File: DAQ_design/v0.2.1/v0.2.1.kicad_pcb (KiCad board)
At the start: 2 copper layers, 48.7 x 79.5 mm, 19 parts, among them J1 Barrel_Jack, J3 Conn_01x04_Female, J4 Conn_01x05_Female, Q1 BC549, Q2 IRF9540N, Q3 IRF540N, Q4 BC549, Q5 IRF9540N, Q6 IRF540N, U3 ADS1115IDGS

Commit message: updated foorprints
updated footprints
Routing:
- net AIN0: track 110.3 -> 114.4 mm
- net VDD: track 41.5 -> 37.5 mm
- net LOGIC1: track 97.2 -> 96.2 mm
- net SP: track 37.4 -> 36.8 mm

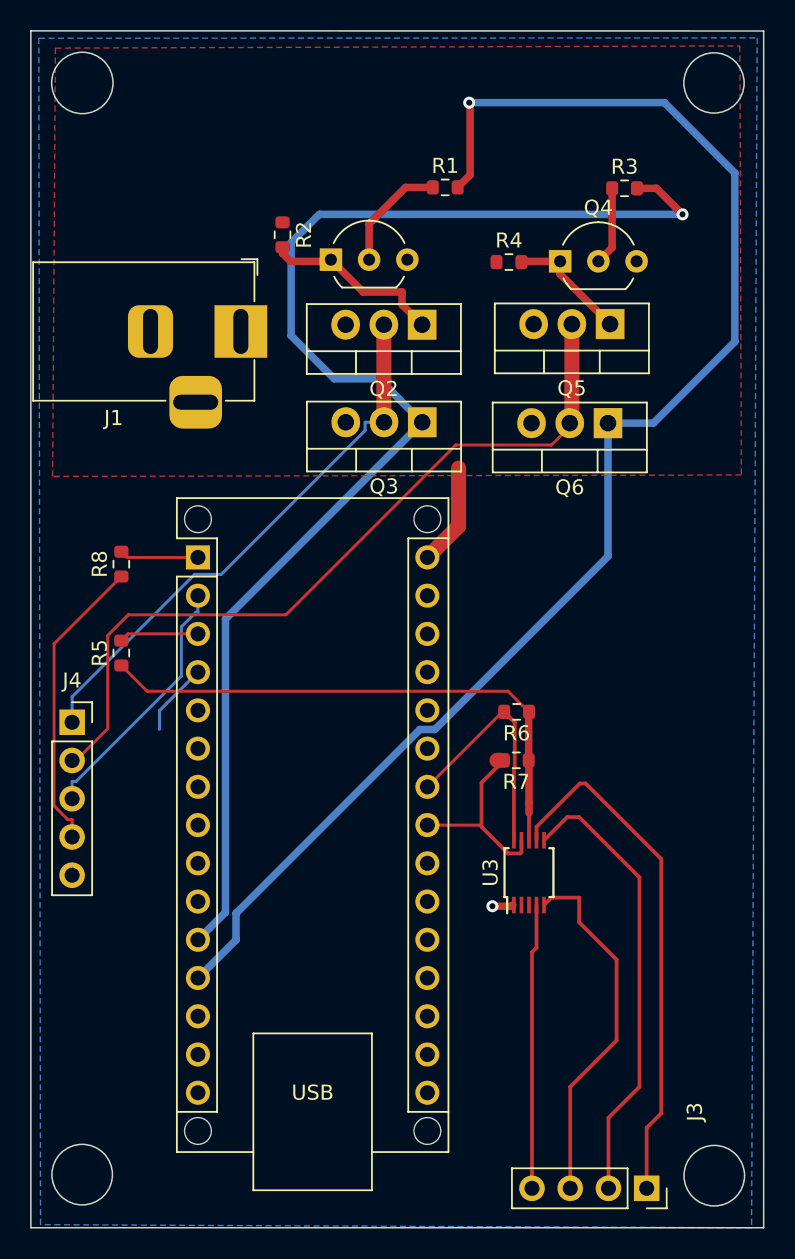
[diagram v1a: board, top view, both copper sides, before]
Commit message: fixed ground plane issue
fixed ground plane issue
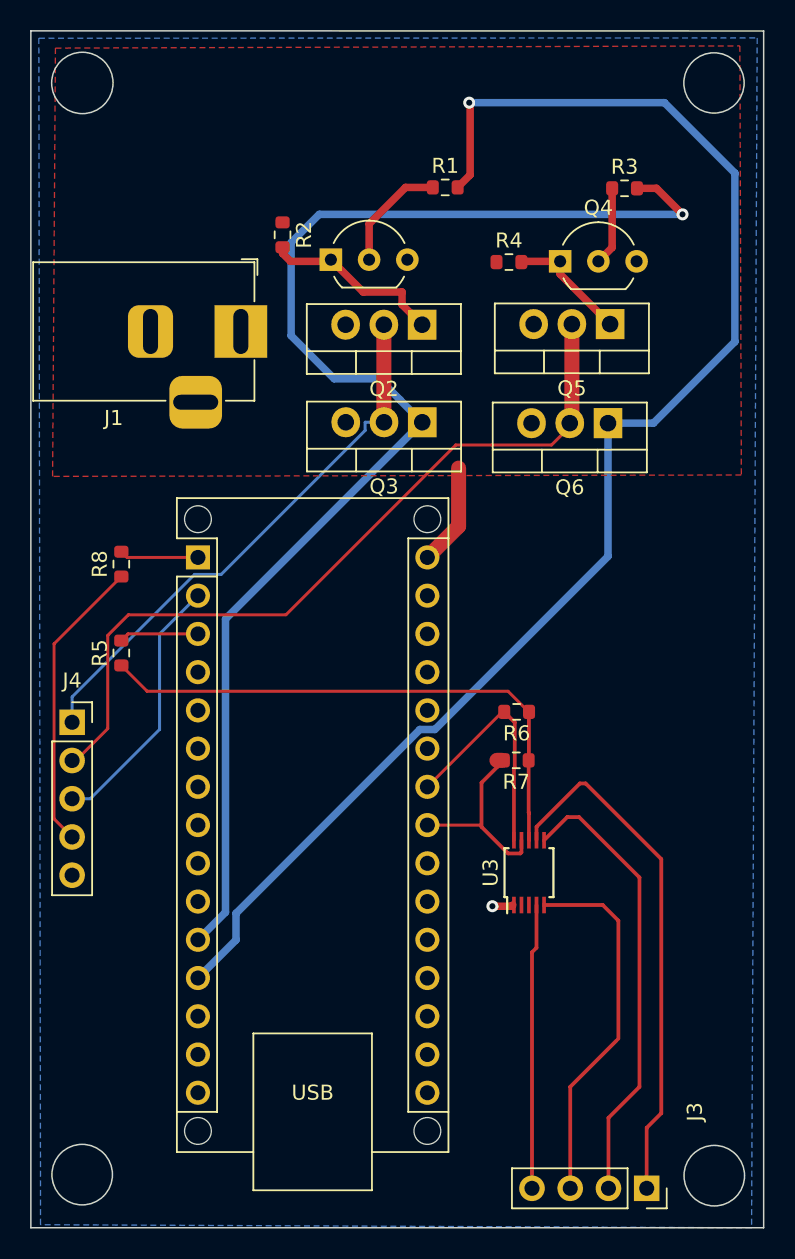
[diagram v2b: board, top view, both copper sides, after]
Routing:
- net AIN0: track 114.4 -> 109.8 mm
- net VDD: track 37.5 -> 37.0 mm
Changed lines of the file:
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@@
   (segment (start 66.485 54.61) (end 71.13 54.61) (width 0.2) (layer "F.Cu") (net 1))
   (segment (start 66.04 55.055) (end 66.485 54.61) (width 0.2) (layer "F.Cu") (net 1))
-  (segment (start 93.1 63.01) (end 93.1 59.815) (width 0.5) (layer "F.Cu") (net 8))
-  (segment (start 93.12 66.51) (end 93.12 65.87) (width 0.25) (layer "F.Cu") (net 8))
+  (segment (start 93.12 66.51) (end 93.1 66.49) (width 0.25) (layer "F.Cu") (net 8))
+  (segment (start 93.1125 62.9975) (end 93.1125 59.8025) (width 0.25) (layer "F.Cu") (net 8))
   (segment (start 91.73 58.42) (end 67.755 58.42) (width 0.2) (layer "F.Cu") (net 8))
+  (segment (start 93.1 63.01) (end 93.1125 62.9975) (width 0.25) (layer "F.Cu") (net 8))
   (segment (start 93.12 68.32) (end 93.12 66.51) (width 0.25) (layer "F.Cu") (net 8))
+  (segment (start 93.1 66.49) (end 93.1 63.01) (width 0.25) (layer "F.Cu") (net 8))
   (segment (start 67.755 58.42) (end 66.04 56.705) (width 0.2) (layer "F.Cu") (net 8))
-  (segment (start 93.12 66.51) (end 93.12 65.87) (width 0.5) (layer "F.Cu") (net 8))
   (segment (start 93.1125 59.8025) (end 91.73 58.42) (width 0.2) (layer "F.Cu") (net 8))
   (segment (start 93.1 59.815) (end 93.1125 59.8025) (width 0.5) (layer "F.Cu") (net 8))
   (segment (start 93.12 63.03) (end 93.1 63.01) (width 0.5) (layer "F.Cu") (net 8))
   (segment (start 93.1125 59.8025) (end 93.125 59.79) (width 0.5) (layer "F.Cu") (net 8))
-  (segment (start 93.12 65.87) (end 93.12 63.03) (width 0.5) (layer "F.Cu") (net 8))
-  (segment (start 96.45 73.76) (end 98.94 76.25) (width 0.25) (layer "F.Cu") (net 9))
   (segment (start 100.46 84.7) (end 100.46 70.79) (width 0.25) (layer "F.Cu") (net 9))
   (segment (start 92.005 72.66) (end 92.045 72.62) (width 0.5) (layer "F.Cu") (net 9))
   (segment (start 98.94 81.62) (end 95.86 84.7) (width 0.25) (layer "F.Cu") (net 9))
   (segment (start 96.885 64.545) (end 96.5 64.545) (width 0.25) (layer "F.Cu") (net 9))
-  (segment (start 94.61 72.13) (end 94.12 72.62) (width 0.25) (layer "F.Cu") (net 9))
   (segment (start 92.08 72.66) (end 92.12 72.62) (width 0.2) (layer "F.Cu") (net 9))
   (segment (start 93.32 75.76) (end 93.62 75.46) (width 0.25) (layer "F.Cu") (net 9))
   (segment (start 100.46 70.79) (end 96.45 66.78) (width 0.25) (layer "F.Cu") (net 9))
   (segment (start 100.94 91.44) (end 100.94 87.42) (width 0.25) (layer "F.Cu") (net 9))
-  (segment (start 96.45 72.13) (end 94.61 72.13) (width 0.25) (layer "F.Cu") (net 9))
-  (segment (start 96.45 72.13) (end 96.45 73.76) (width 0.25) (layer "F.Cu") (net 9))
+  (segment (start 99.06 81.5) (end 98.94 81.62) (width 0.2) (layer "F.Cu") (net 9))
   (segment (start 96.5 64.545) (end 93.62 67.425) (width 0.25) (layer "F.Cu") (net 9))
   (segment (start 93.62 67.425) (end 93.62 68.32) (width 0.25) (layer "F.Cu") (net 9))
@@
   (segment (start 93.62 72.62) (end 93.62 75.46) (width 0.25) (layer "F.Cu") (net 9))
   (segment (start 101.91 69.57) (end 96.885 64.545) (width 0.25) (layer "F.Cu") (net 9))
-  (segment (start 98.94 76.25) (end 98.94 81.62) (width 0.25) (layer "F.Cu") (net 9))
   (segment (start 101.91 86.45) (end 101.91 69.57) (width 0.25) (layer "F.Cu") (net 9))
   (segment (start 91.965 72.7) (end 92.005 72.66) (width 0.5) (layer "F.Cu") (net 9))
+  (segment (start 94.12 72.62) (end 98.02 72.62) (width 0.25) (layer "F.Cu") (net 9))
   (segment (start 100.94 87.42) (end 101.91 86.45) (width 0.25) (layer "F.Cu") (net 9))
   (segment (start 98.4 86.76) (end 100.46 84.7) (width 0.25) (layer "F.Cu") (net 9))
+  (segment (start 98.02 72.62) (end 99.06 73.66) (width 0.25) (layer "F.Cu") (net 9))
   (segment (start 92.005 72.66) (end 92.08 72.66) (width 0.2) (layer "F.Cu") (net 9))
   (segment (start 98.4 91.44) (end 98.4 86.76) (width 0.25) (layer "F.Cu") (net 9))
+  (segment (start 99.06 73.66) (end 99.06 81.5) (width 0.25) (layer "F.Cu") (net 9))
   (via (at 90.69 72.7) (size 0.8) (drill 0.4) (layers "F.Cu" "B.Cu") (net 9))
-  (segment (start 71.13 57.15) (end 68.58 59.7) (width 0.2) (layer "B.Cu") (net 9))
-  (segment (start 68.58 59.7) (end 68.58 60.96) (width 0.2) (layer "B.Cu") (net 9))
   (segment (start 88.4437 47.4563) (end 86.37 49.53) (width 1) (layer "F.Cu") (net 10))
   (segment (start 88.4437 43.596) (end 88.4437 47.4563) (width 1) (layer "F.Cu") (net 10))
@@
   (segment (start 106.8 24) (end 106.8 35.2) (width 0.5) (layer "B.Cu") (net 15))
   (segment (start 106.8 35.2) (end 101.39 40.61) (width 0.5) (layer "B.Cu") (net 15))
-  (segment (start 63.0385 64.4081) (end 62.77 64.4081) (width 0.2) (layer "B.Cu") (net 16))
-  (segment (start 70.0281 54.1359) (end 70.0281 57.4185) (width 0.2) (layer "B.Cu") (net 16))
-  (segment (start 71.13 53.1719) (end 70.9921 53.1719) (width 0.2) (layer "B.Cu") (net 16))
-  (segment (start 71.13 52.07) (end 71.13 53.1719) (width 0.2) (layer "B.Cu") (net 16))
-  (segment (start 70.9921 53.1719) (end 70.0281 54.1359) (width 0.2) (layer "B.Cu") (net 16))
-  (segment (start 70.0281 57.4185) (end 63.0385 64.4081) (width 0.2) (layer "B.Cu") (net 16))
-  (segment (start 62.77 64.4081) (end 62.77 65.56) (width 0.2) (layer "B.Cu") (net 16))
+  (segment (start 68.58 60.96) (end 63.98 65.56) (width 0.2) (layer "B.Cu") (net 16))
+  (segment (start 63.98 65.56) (end 62.77 65.56) (width 0.2) (layer "B.Cu") (net 16))
+  (segment (start 71.13 52.07) (end 68.58 54.62) (width 0.2) (layer "B.Cu") (net 16))
+  (segment (start 68.58 54.62) (end 68.58 60.96) (width 0.2) (layer "B.Cu") (net 16))
   (segment (start 92.62 69.12) (end 92.62 68.32) (width 0.25) (layer "F.Cu") (net 27))
   (segment (start 92.545 69.195) (end 92.62 69.12) (width 0.25) (layer "F.Cu") (net 27))
@@
   (segment (start 91.35 59.79) (end 91.475 59.79) (width 0.25) (layer "F.Cu") (net 28))
   (segment (start 86.37 64.77) (end 91.35 59.79) (width 0.2) (layer "F.Cu") (net 28))
-  (segment (start 61.5715 66.0376) (end 61.5715 55.2685) (width 0.2) (layer "F.Cu") (net 33))
-  (segment (start 62.482 66.9481) (end 61.5715 66.0376) (width 0.2) (layer "F.Cu") (net 33))
-  (segment (start 62.77 66.9481) (end 62.482 66.9481) (width 0.2) (layer "F.Cu") (net 33))
-  (segment (start 62.77 68.1) (end 62.77 66.9481) (width 0.2) (layer "F.Cu") (net 33))
-  (segment (start 61.5715 55.2685) (end 66.04 50.8) (width 0.2) (layer "F.Cu") (net 33))
+  (segment (start 66.04 50.8) (end 61.5715 55.2685) (width 0.2) (layer "F.Cu") (net 33))
+  (segment (start 61.5715 55.2685) (end 61.5715 66.9015) (width 0.2) (layer "F.Cu") (net 33))
+  (segment (start 61.5715 66.9015) (end 62.77 68.1) (width 0.2) (layer "F.Cu") (net 33))
   (segment (start 84.92 24.95) (end 86.73 24.95) (width 0.5) (layer "F.Cu") (net 34))
   (segment (start 82.5 29.75) (end 82.5 27.37) (width 0.5) (layer "F.Cu") (net 34))
